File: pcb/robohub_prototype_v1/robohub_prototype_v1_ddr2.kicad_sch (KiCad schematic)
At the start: 39 parts, among them U1 ATSAMA5D27C, U31 W972GG6KB-25, U32 W972GG6KB-25

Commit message: Update paths to footprint libraries. Begin adding footprints for PDN resistors. Create master BOM
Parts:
- U1: footprint custom_footprint:SAMA5D27C-CNVAO -> fryelabs:ATSAMA5D27C
- U31, U32: footprint custom_footprint:W972GG6KB-25 -> fryelabs:W972GG6KB-25
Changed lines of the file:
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@@
 			)
 		)
-		(property "Footprint" "custom_footprint:W972GG6KB-25"
+		(property "Footprint" "fryelabs:W972GG6KB-25"
 			(at 71.12 86.36 0)
 			(effects
@@
 			)
 		)
-		(property "Footprint" "custom_footprint:W972GG6KB-25"
+		(property "Footprint" "fryelabs:W972GG6KB-25"
 			(at 191.77 86.36 0)
 			(effects
@@
 			)
 		)
-		(property "Footprint" "custom_footprint:SAMA5D27C-CNVAO"
+		(property "Footprint" "fryelabs:ATSAMA5D27C"
 			(at 55.118 359.664 0)
 			(effects

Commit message: Begin PDN circuit design/BOM/layout
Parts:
- R35, R36: footprint (none) -> Resistor_SMD:R_0402_1005Metric
- U1: footprint fryelabs:ATSAMA5D27C -> fryelabs_kicad_footprint_lib:ATSAMA5D27C
- U31, U32: footprint fryelabs:W972GG6KB-25 -> fryelabs_kicad_footprint_lib:W972GG6KB-25
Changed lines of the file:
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@@
 			)
 		)
-		(property "Footprint" "fryelabs:W972GG6KB-25"
+		(property "Footprint" "fryelabs_kicad_footprint_lib:W972GG6KB-25"
 			(at 71.12 86.36 0)
 			(effects
@@
 			)
 		)
-		(property "Footprint" "fryelabs:W972GG6KB-25"
+		(property "Footprint" "fryelabs_kicad_footprint_lib:W972GG6KB-25"
 			(at 191.77 86.36 0)
 			(effects
@@
 			)
 		)
-		(property "Footprint" ""
+		(property "Footprint" "Resistor_SMD:R_0402_1005Metric"
 			(at 89.662 210.82 90)
 			(effects
@@
 			)
 		)
-		(property "Footprint" ""
+		(property "Footprint" "Resistor_SMD:R_0402_1005Metric"
 			(at 102.362 205.74 90)
 			(effects
@@
 			)
 		)
-		(property "Footprint" "fryelabs:ATSAMA5D27C"
+		(property "Footprint" "fryelabs_kicad_footprint_lib:ATSAMA5D27C"
 			(at 55.118 359.664 0)
 			(effects

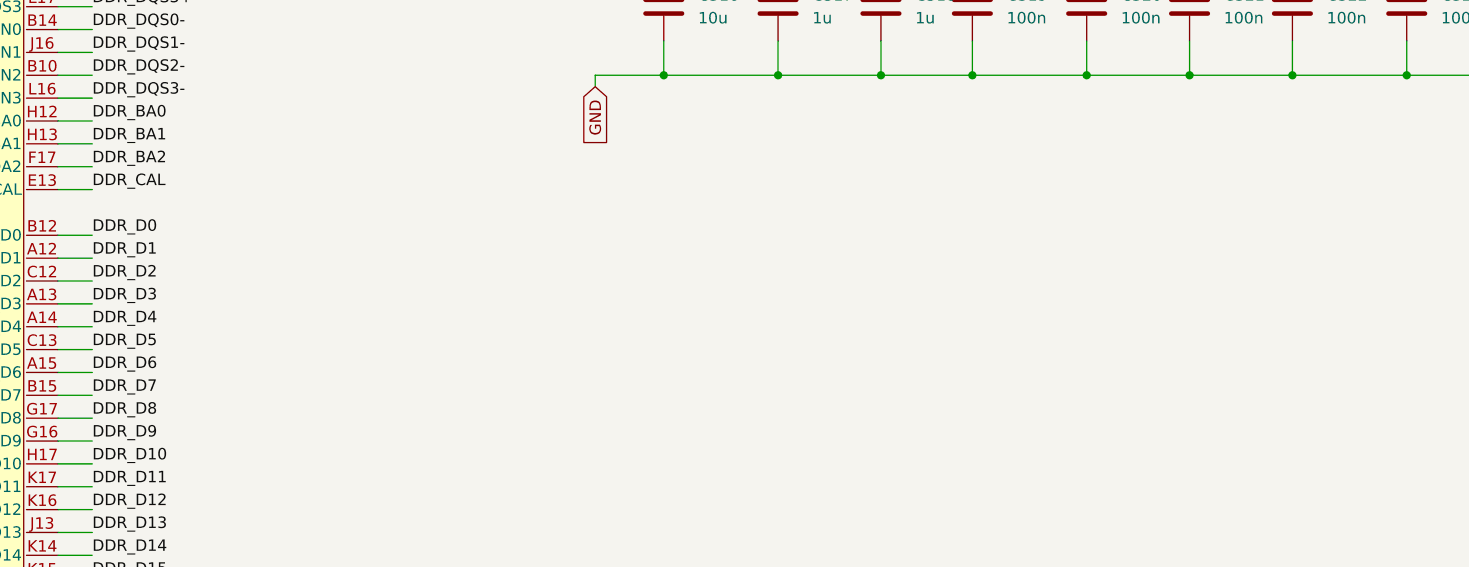
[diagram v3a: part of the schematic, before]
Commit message: Small updates to ACC signals for DDR2
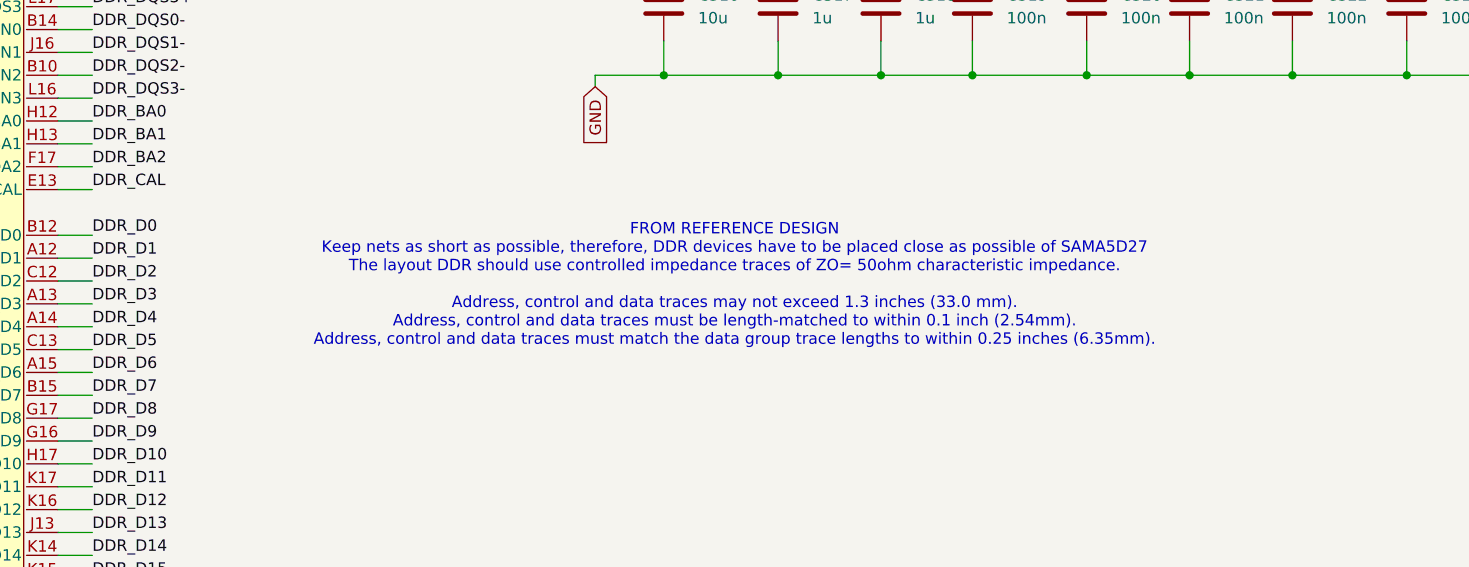
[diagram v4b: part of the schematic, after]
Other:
- note added: "FROM REFERENCE DESIGN Keep nets as short as possible, therefore, DDR devices have to be placed close as possible of SAMA5D27 The layout DDR should use controlled impedance traces of ZO= 50ohm characteristic impedance. Address, control and data traces may not exceed 1.3 inches (33.0 mm). Address, control and data traces must be length-matched to within 0.1 inch (2.54mm). Address, control and data 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"
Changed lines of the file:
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@@
+		)
+	)
+	(text "FROM REFERENCE DESIGN\nKeep nets as short as possible, therefore, DDR devices have to be placed close as possible of SAMA5D27\nThe layout DDR should use controlled impedance traces of ZO= 50ohm characteristic impedance.\n\nAddress, control and data traces may not exceed 1.3 inches (33.0 mm).\nAddress, control and data traces must be length-matched to within 0.1 inch (2.54mm).\nAddress, control and data traces must match the data group trace lengths to within 0.25 inches (6.35mm)."
+		(exclude_from_sim no)
+		(at 145.034 278.638 0)
+		(effects
+			(font
+				(size 1.27 1.27)
+			)
 		)
 	)

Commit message: Update pcb with decoupling, updated winbond ddr footprint. added some decoupling caps
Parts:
- C316, C317, C318, C35, C36, C37, C38, C39: footprint (none) -> Capacitor_SMD:C_0402_1005Metric
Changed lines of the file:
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@@
 			)
 		)
-		(property "Footprint" ""
+		(property "Footprint" "Capacitor_SMD:C_0402_1005Metric"
 			(at 185.1152 212.09 0)
 			(effects
@@
 			)
 		)
-		(property "Footprint" ""
+		(property "Footprint" "Capacitor_SMD:C_0402_1005Metric"
 			(at 138.1252 212.09 0)
 			(effects
@@
 			)
 		)
-		(property "Footprint" ""
+		(property "Footprint" "Capacitor_SMD:C_0402_1005Metric"
 			(at 150.8252 251.46 0)
 			(effects
@@
 			)
 		)
-		(property "Footprint" ""
+		(property "Footprint" "Capacitor_SMD:C_0402_1005Metric"
 			(at 162.2552 212.09 0)
 			(effects
@@
 			)
 		)
-		(property "Footprint" ""
+		(property "Footprint" "Capacitor_SMD:C_0402_1005Metric"
 			(at 162.2552 251.46 0)
 			(effects
@@
 			)
 		)
-		(property "Footprint" ""
+		(property "Footprint" "Capacitor_SMD:C_0402_1005Metric"
 			(at 150.8252 212.09 0)
 			(effects
@@
 			)
 		)
-		(property "Footprint" ""
+		(property "Footprint" "Capacitor_SMD:C_0402_1005Metric"
 			(at 172.4152 212.09 0)
 			(effects
@@
 			)
 		)
-		(property "Footprint" ""
+		(property "Footprint" "Capacitor_SMD:C_0402_1005Metric"
 			(at 138.1252 251.46 0)
 			(effects

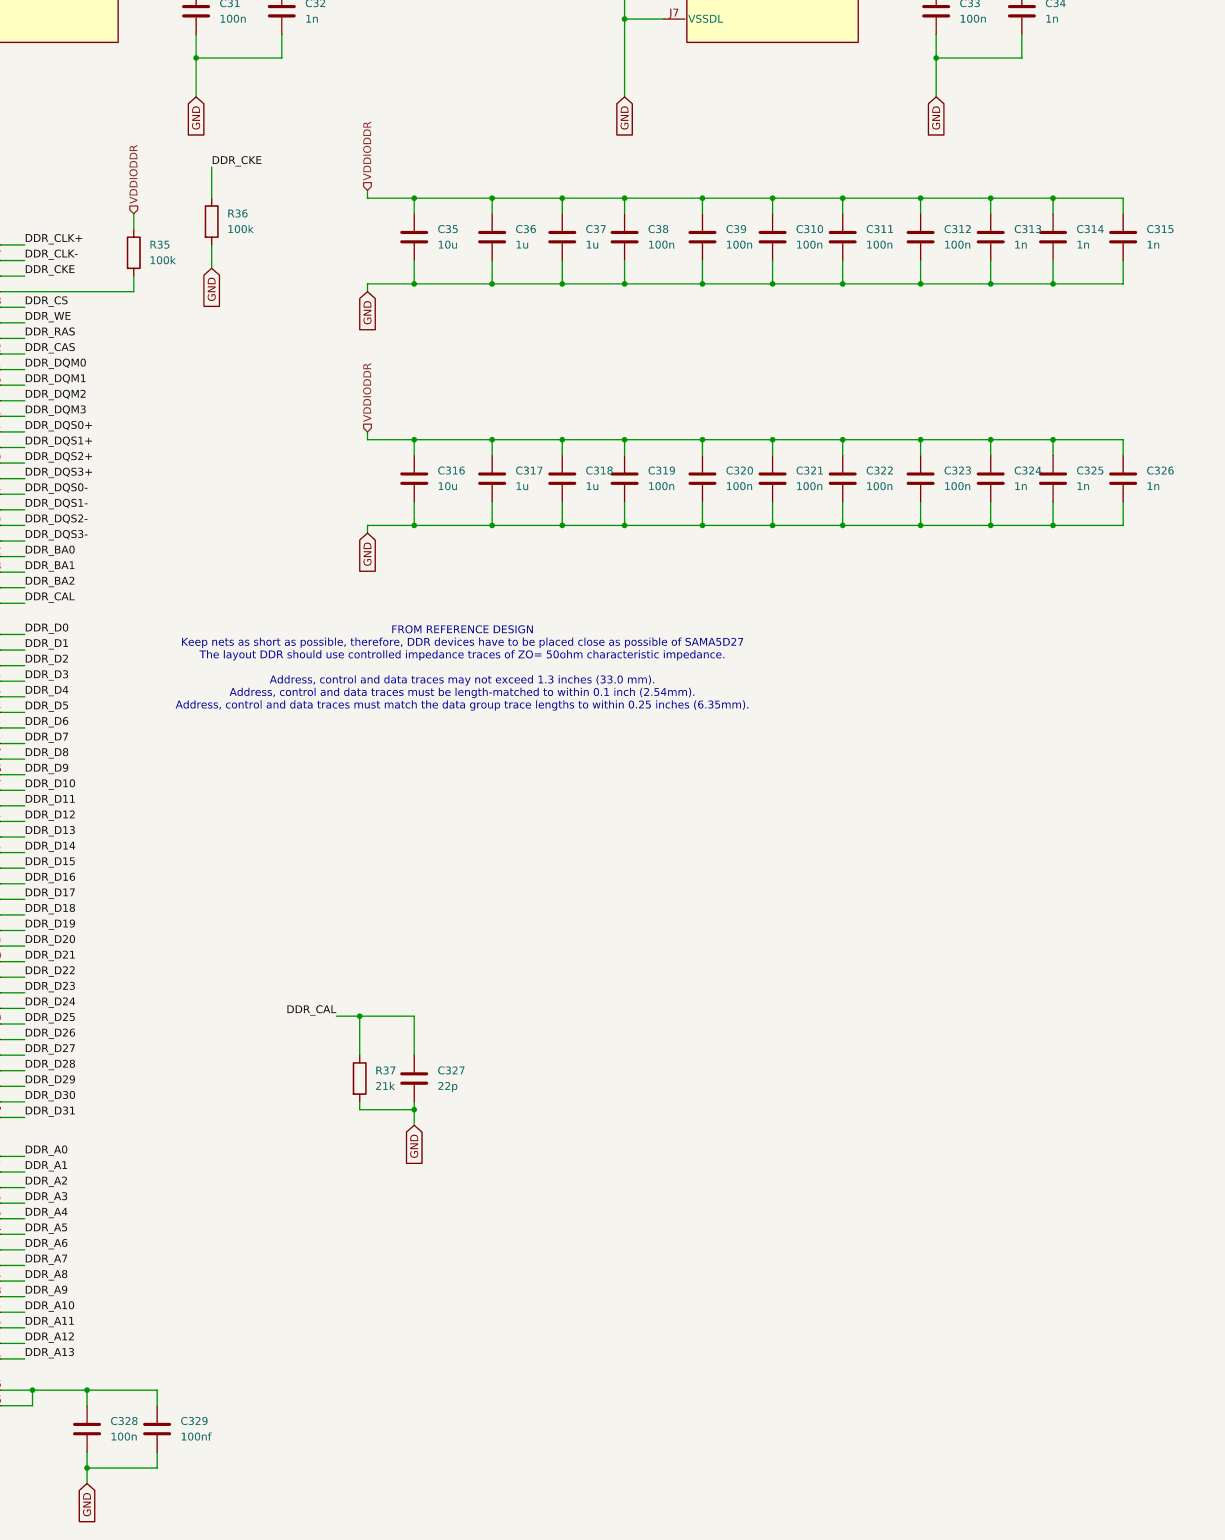
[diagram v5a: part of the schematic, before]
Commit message: Add changes for docoupling capacitors
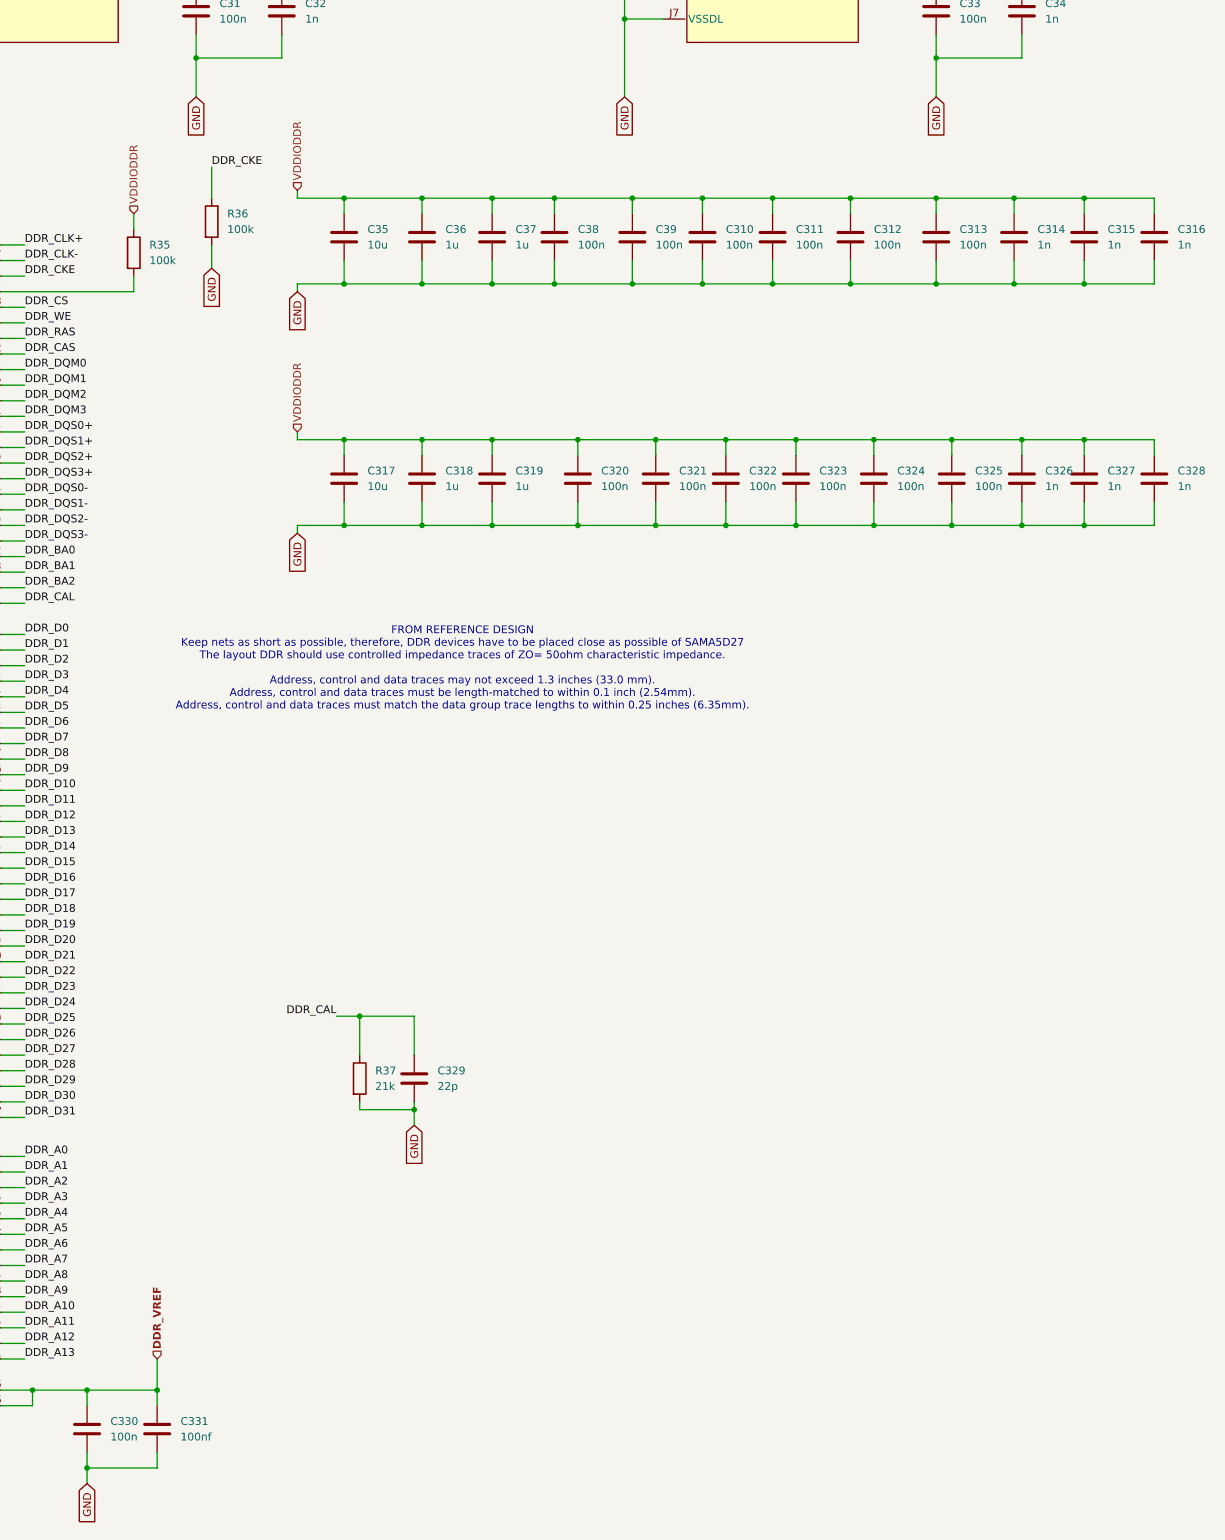
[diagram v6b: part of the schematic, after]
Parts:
- added C313, C325: 100n, Capacitor_SMD:C_0402_1005Metric, symbol Device:C
- C310, C311, C312, C33, C34: footprint (none) -> Capacitor_SMD:C_0402_1005Metric
- C314: renamed from C313; footprint (none) -> Capacitor_SMD:C_0402_1005Metric
- C315: renamed from C314; footprint (none) -> Capacitor_SMD:C_0402_1005Metric
- C316: renamed from C315; footprint (none) -> Capacitor_SMD:C_0402_1005Metric
- C320: renamed from C319; footprint (none) -> Capacitor_SMD:C_0402_1005Metric
- C321: renamed from C320; footprint (none) -> Capacitor_SMD:C_0402_1005Metric
- C322: renamed from C321; footprint (none) -> Capacitor_SMD:C_0402_1005Metric
- C323: renamed from C322; footprint (none) -> Capacitor_SMD:C_0402_1005Metric
- C324: renamed from C323; footprint (none) -> Capacitor_SMD:C_0402_1005Metric
- C326: renamed from C324; footprint (none) -> Capacitor_SMD:C_0402_1005Metric
- C327: renamed from C325; footprint (none) -> Capacitor_SMD:C_0402_1005Metric
- C328: renamed from C326; footprint (none) -> Capacitor_SMD:C_0402_1005Metric
- C330: renamed from C328; footprint (none) -> Capacitor_SMD:C_0402_1005Metric
- C331: renamed from C329; footprint (none) -> Capacitor_SMD:C_0402_1005Metric
- renumbered C316 to C317, C317 to C318, C318 to C319, C327 to C329
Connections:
- net DDR_VREF: now also C330.1, C331.1, U1.D16 (DDR_VREF), U1.H16 (DDR_VREF)
- net GND: now also C313.2, C325.2
- net VDDIODDR: now also C313.1, C325.1
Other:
- moved on the sheet: C310, C311, C312, C314, C315, C316, C317, C318, C319, C320, C321, C322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
